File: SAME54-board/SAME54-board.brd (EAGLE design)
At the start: 55.3 x 107.2 mm, 31 parts, among them IC1 ATSAME54N20A-AUT, J1 GSD09002SEU, J2 CON-SOCJ-2155

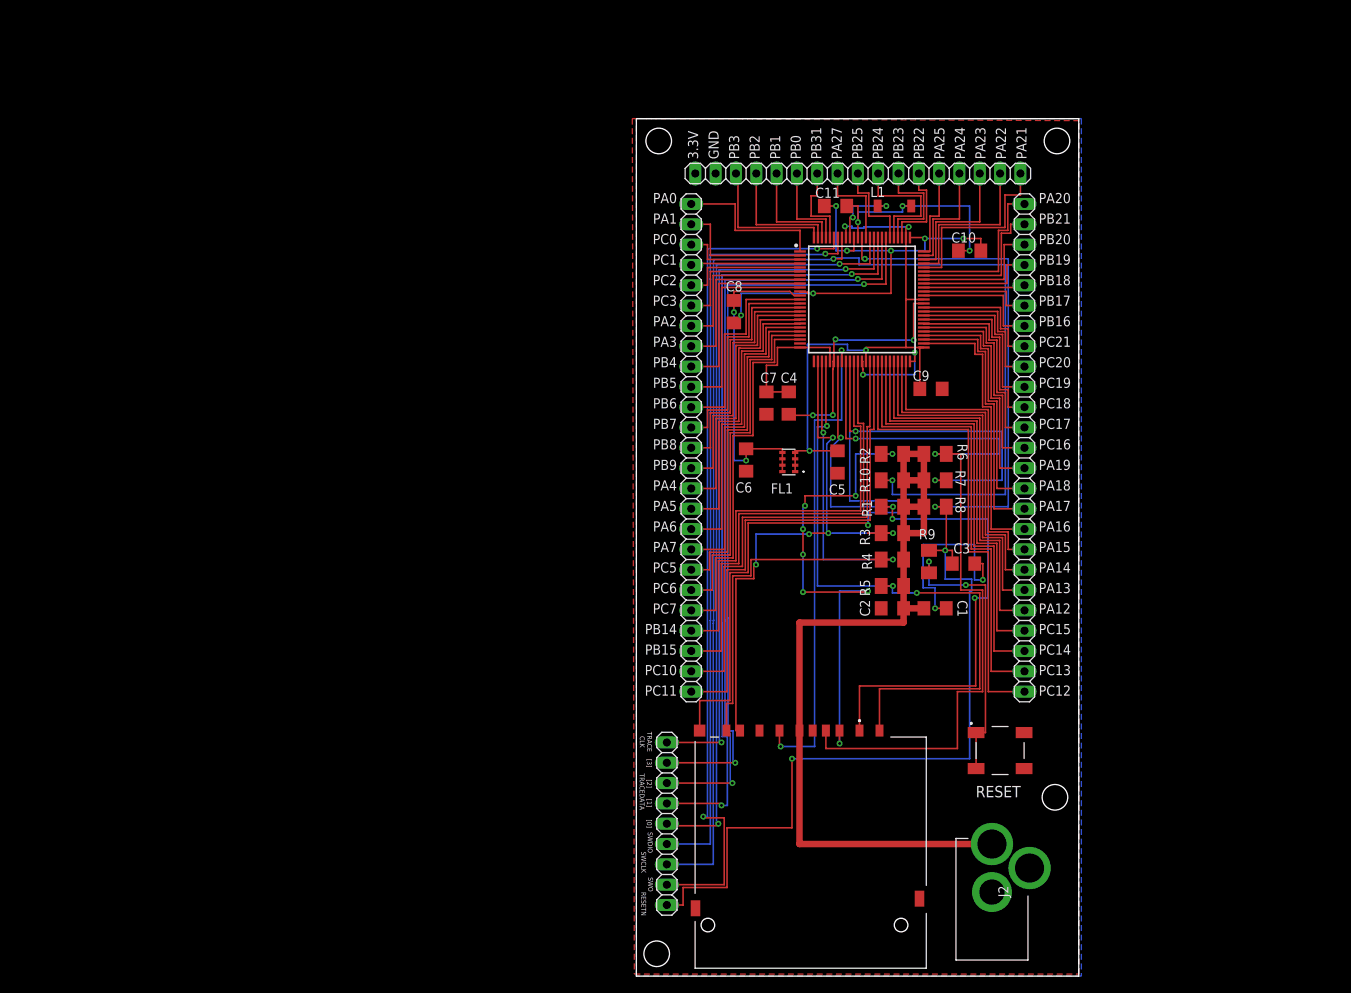
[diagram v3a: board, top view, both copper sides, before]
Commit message: Starting new version of board. Bought Microchip development board--will only be printing final product
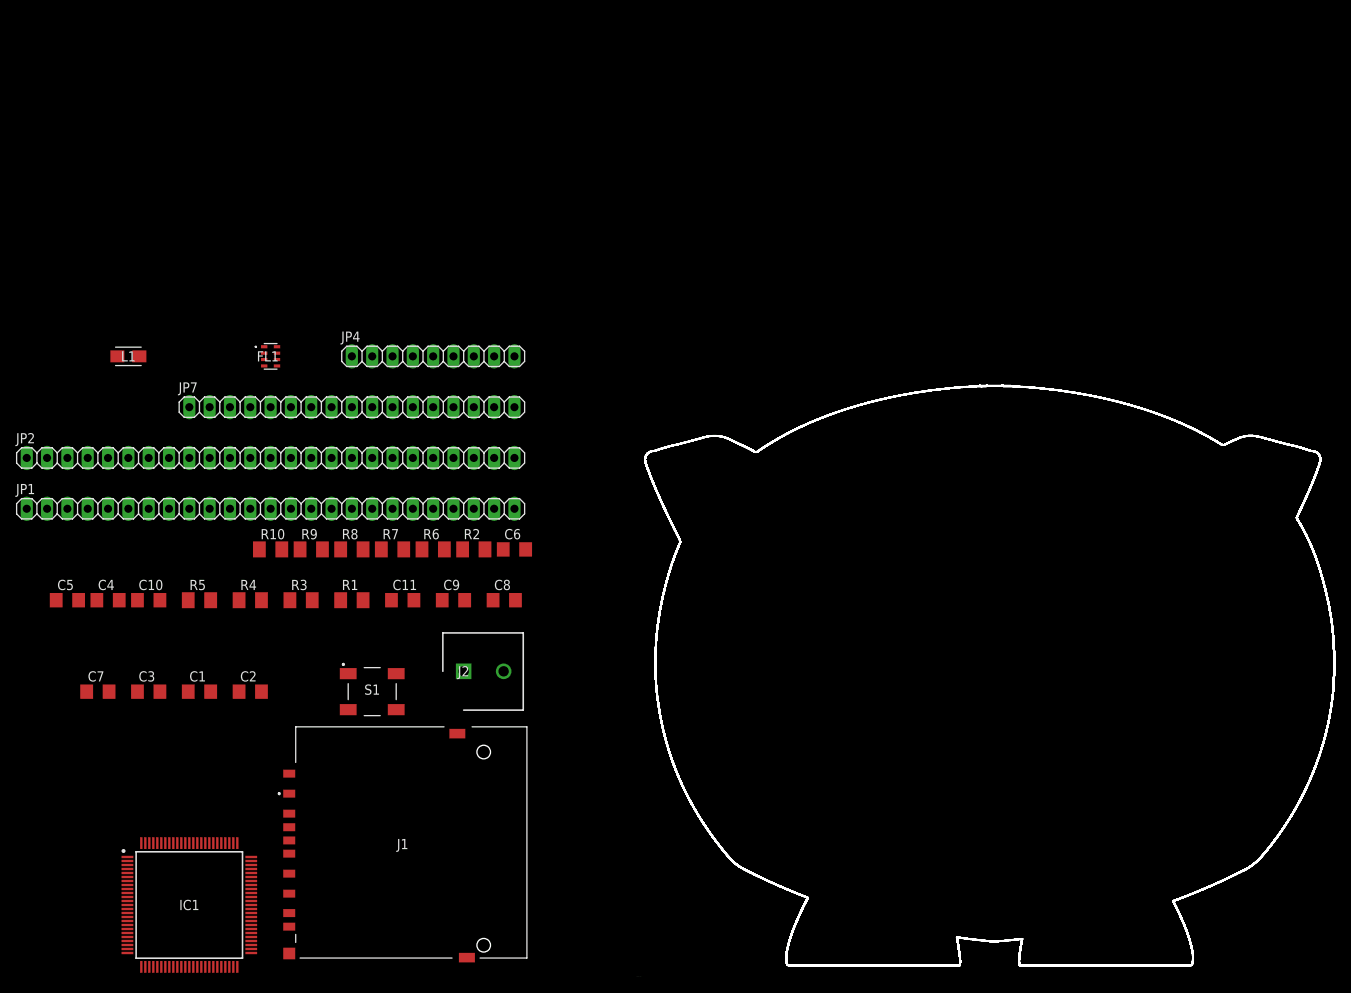
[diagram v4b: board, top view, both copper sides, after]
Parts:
- J2: value CON-SOCJ-2155 -> 1985920; device SamacSys_Parts:CONSOCJ2155 -> SamacSys_Parts:SHDR2W110P0X500_1X2_1000X950X1
- L1: value 10uH -> LQH31MN100J03L; device rcl:L4516C -> SamacSys_Parts:LQH31CN100K03L
- moved IC1 113.1 mm to (-55.9, 8.89)
- moved C10 111.5 mm to (-61.0, 47.0)
- moved C3 103.1 mm to (-61.0, 35.6)
- moved C5 97.8 mm to (-71.1, 47.0), turned to 0 degrees
- moved L1 97.6 mm to (-63.5, 77.5), turned to 0 degrees
- moved JP1 95.9 mm to (-47.0, 58.4), turned to 0 degrees
- moved C1 92.5 mm to (-54.6, 35.6)
- moved C7 91.0 mm to (-67.3, 35.6), turned to 0 degrees
- moved C4 88.6 mm to (-66.0, 47.0), turned to 0 degrees
- moved R5 86.6 mm to (-54.6, 47.0)
- moved C2 80.9 mm to (-48.3, 35.6), turned to 0 degrees
- moved R4 80.4 mm to (-48.3, 47.0)
- moved S1 78.8 mm to (-33.0, 35.6)
- moved R10 78.2 mm to (-45.7, 53.3)
- moved R9 77.2 mm to (-40.6, 53.3), turned to 0 degrees
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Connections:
- net N$24 renamed PA21
- net N$25 renamed PA22
- net N$27 renamed PA24
- net N$28 renamed PA25
- net N$59 renamed PB31
- net N$60 renamed PB0
- net N$61 renamed PB1
- net N$62 renamed PB3
- net N$63 renamed PB2
- net N$64 renamed PB22
- net N$65 renamed PB23
- net N$66 renamed PB24
- net N$67 renamed PB25
- net N$68 renamed PA27
- net GND: now also S1.1; no longer J2.3, S1.4
- net N$4: now also S1.4; no longer S1.1
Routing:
- net SWDCLK: track 168.7 -> 0.00 mm, vias 2 -> 0
- net RESETN: track 158.2 -> 0.00 mm, vias 4 -> 0
- net GND: track 134.6 -> 0.00 mm, vias 15 -> 0
- net SDWP: track 113.4 -> 0.00 mm, vias 3 -> 0
- net VCC: track 108.4 -> 0.00 mm
- net SWO: track 106.9 -> 0.00 mm, vias 2 -> 0
- net SDCD: track 103.4 -> 0.00 mm, vias 2 -> 0
- net TRACEDATA[0]: track 99.6 -> 0.00 mm, vias 2 -> 0
- net TRACEDATA[1]: track 98.9 -> 0.00 mm, vias 2 -> 0
- net SWDIO: track 97.2 -> 0.00 mm, vias 1 -> 0
- net TRACEDATA[2]: track 96.9 -> 0.00 mm, vias 2 -> 0
- net TRACEDATA[3]: track 94.9 -> 0.00 mm, vias 2 -> 0
- net TRACECLK: track 89.5 -> 0.00 mm, vias 2 -> 0
- net SDDAT[3]: track 84.6 -> 0.00 mm, vias 4 -> 0
- net SDDAT[2]: track 81.8 -> 0.00 mm, vias 3 -> 0
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- removed copper zone on layer 1, net GND
- removed copper zone on layer 16, net VCC
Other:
- board size 55.3 x 107.2 mm -> 86.2 x 72.6 mm
- board text added: "C:/Users/Kris/Desktop/LAMS/lams-logo_PCB-OUTLINE.bmp"
- board text removed: "3.3V GND PB3 PB2 PB1 PB0 PB31 PA27 PB25 PB24 PB23 PB22 PA25 PA24 PA23 PA22 PA21"
- board text removed: "PA0 PA1 PC0 PC1 PC2 PC3 PA2 PA3 PB4 PB5 PB6 PB7 PB8 PB9 PA4 PA5 PA6 PA7 PC5 PC6 PC7 PB14 PB15 PC10 PC11"
- board text removed: "PA20 PB21 PB20 PB19 PB18 PB17 PB16 PC21 PC20 PC19 PC18 PC17 PC16 PA19 PA18 PA17 PA16 PA15 PA14 PA13 PA12 PC15 PC14 PC13 PC12"
- board text removed: "RESET"
- board text removed: "RESETN"
- board text removed: "SWCLK"
- board text removed: "SWDIO"
- board text removed: "SWO"
- board text removed: "TRACE CLK"
- board text removed: "TRACEDATA"
- board text removed: "[0]"
- board text removed: "[1]"
- board text removed: "[2]"
- board text removed: "[3]"
